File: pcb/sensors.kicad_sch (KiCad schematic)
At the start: 10 parts, among them U11 INA230AIRGTR, U12 MCP9804T-E/MC, U13 INA230AIRGTR, U14 INA230AIRGTR

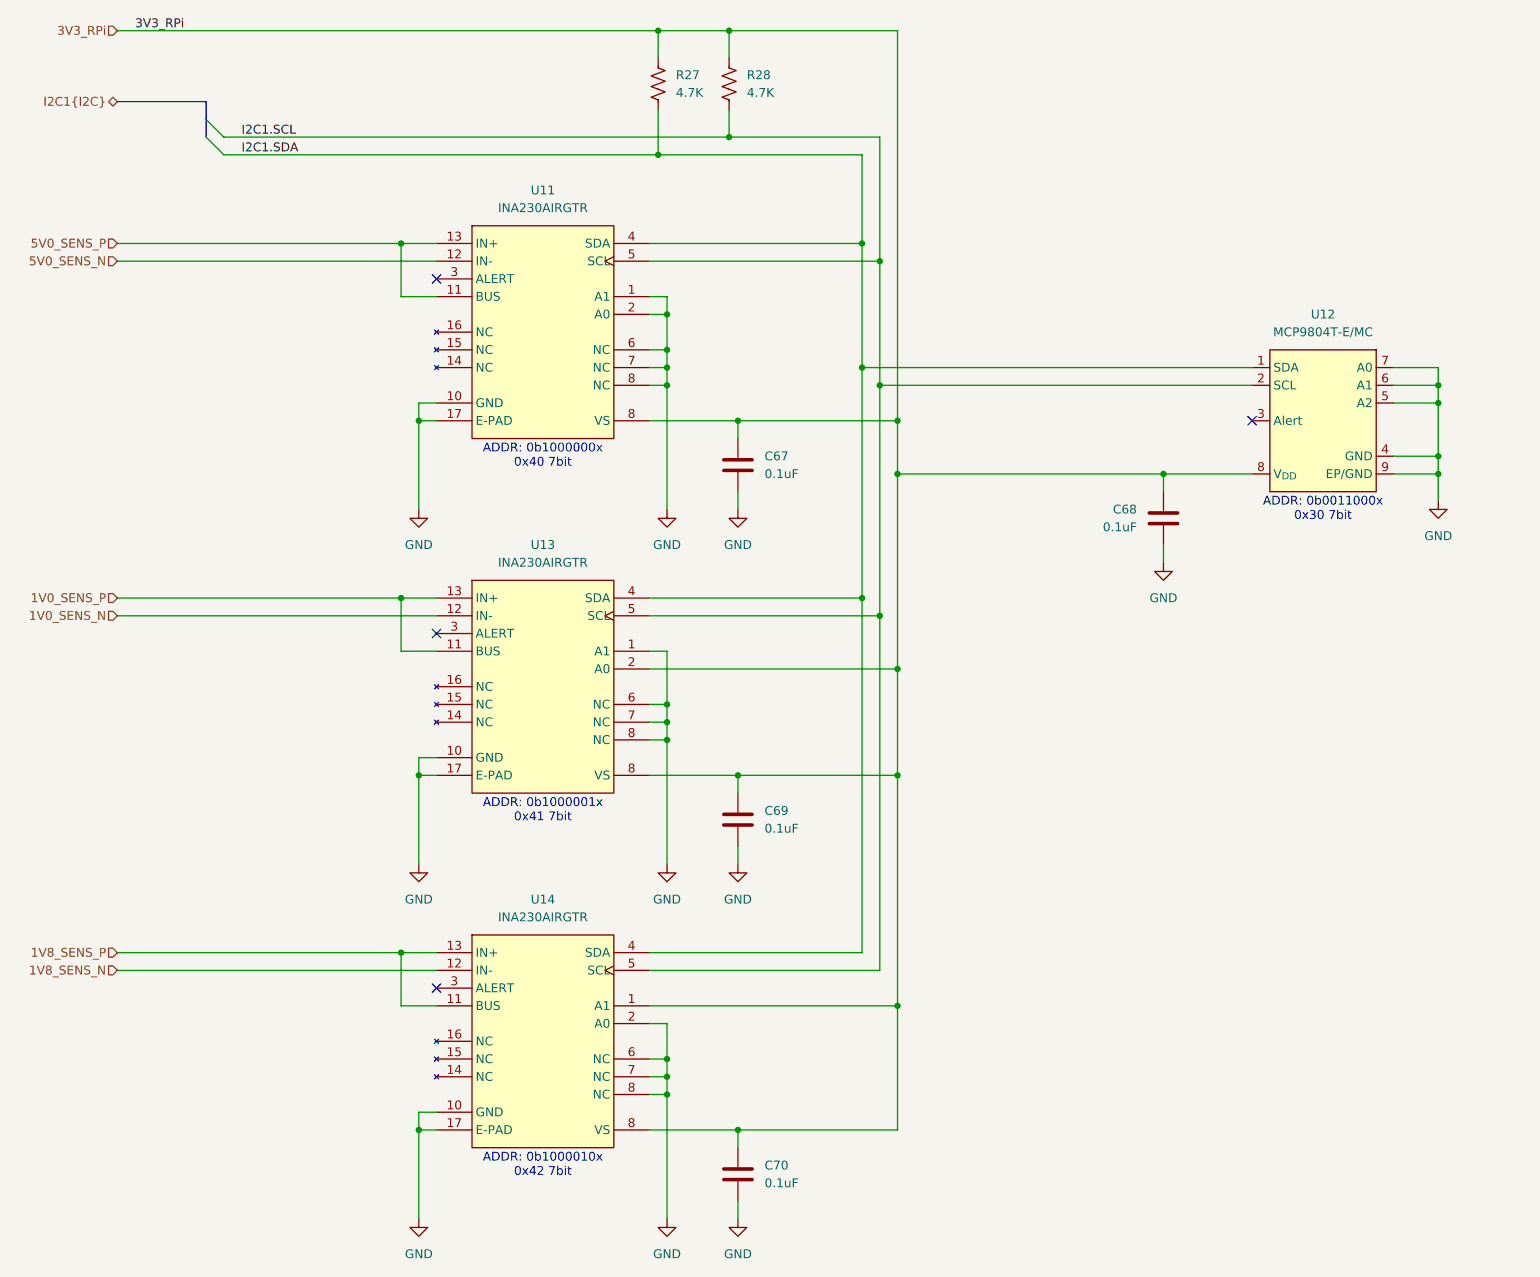
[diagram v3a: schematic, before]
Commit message: restructured power, power plane layout
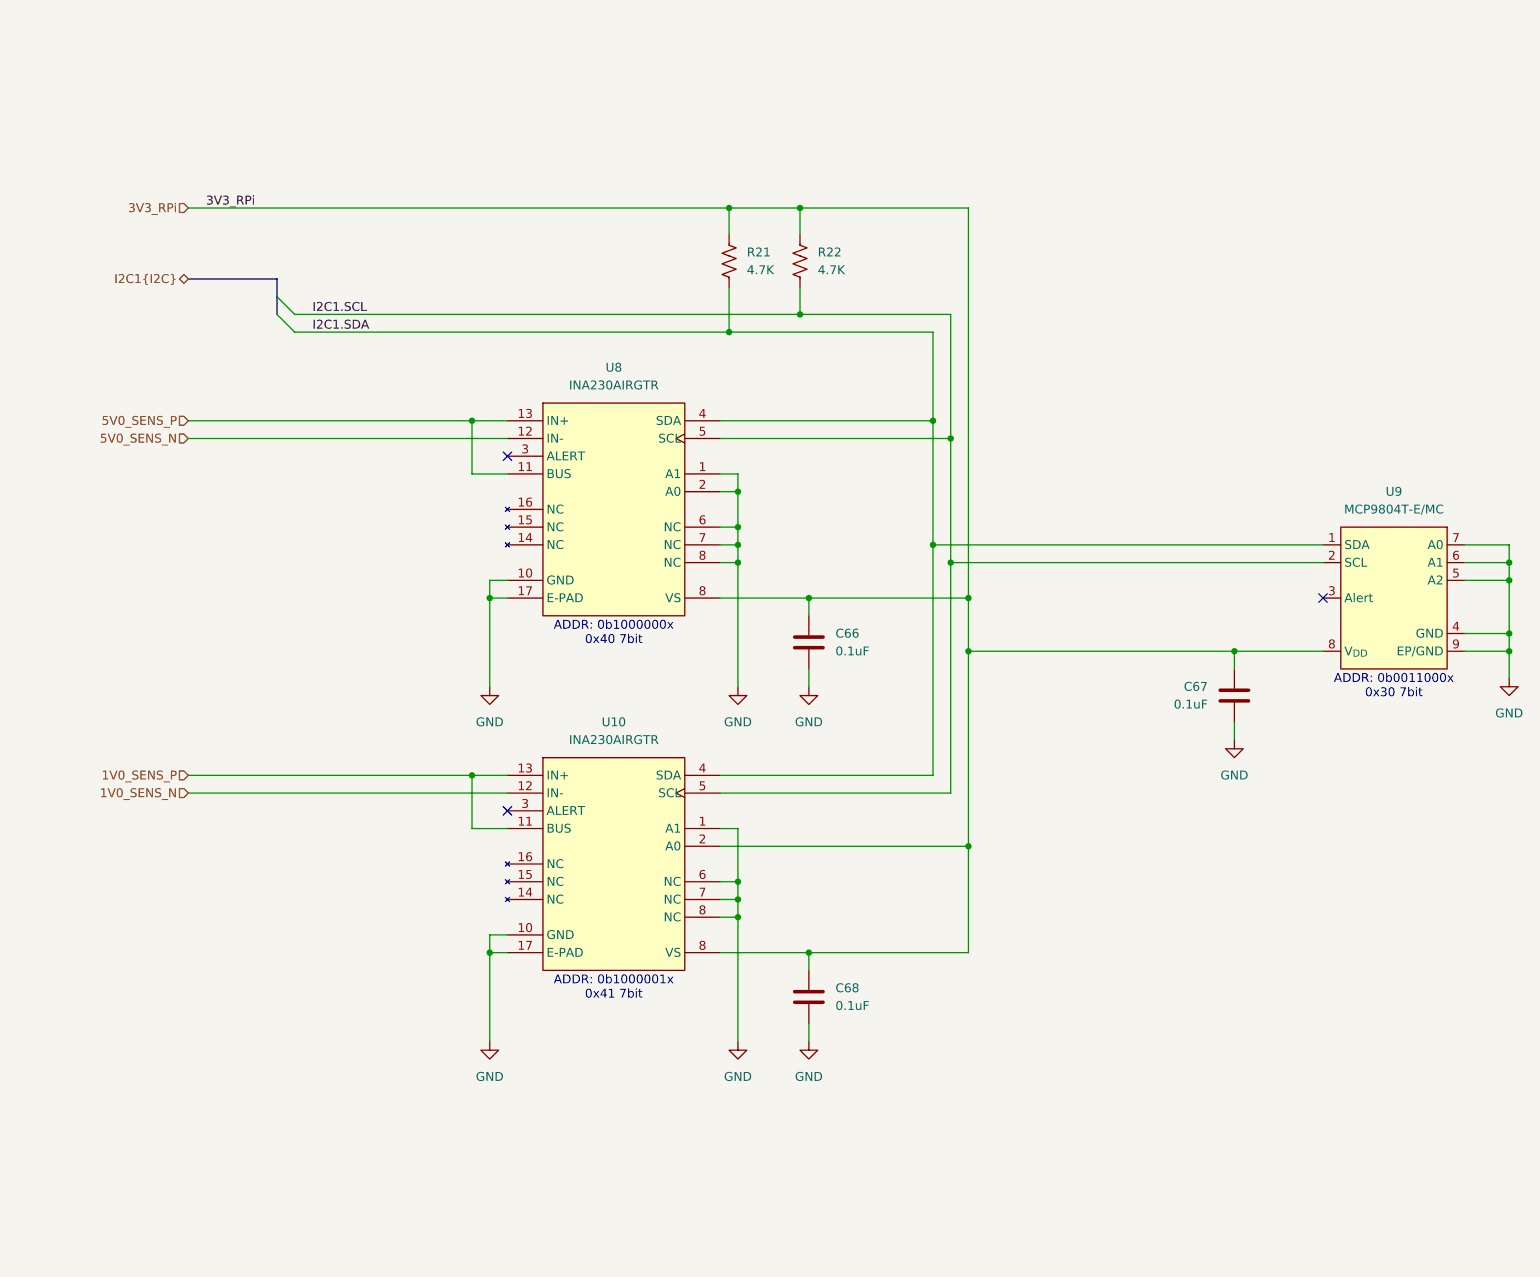
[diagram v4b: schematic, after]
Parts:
- removed C70: 0.1uF, Capacitor_SMD:C_0402_1005Metric, symbol Device:C
- removed U14: INA230AIRGTR, Package_DFN_QFN:VQFN-16-1EP_3x3mm_P0.5mm_EP1.6x1.6mm, symbol library:INA230AIRGTT
- renumbered C67 to C66, C68 to C67, C69 to C68, R27 to R21, R28 to R22, U13 to U10, U11 to U8, U12 to U9
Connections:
- no-connect marks 4 -> 3
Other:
- note removed: "ADDR: 0b1000010x 0x42 7bit"
- moved on the sheet: C66, C67, C68, R21, R22, U10, U8, U9
